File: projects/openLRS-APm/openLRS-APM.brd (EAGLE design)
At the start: 43.1 x 21.8 mm, 23 parts, among them IC2 RFM23BPSMD, J1 AVR_SPI_PRG_6PTH, U1 ATMEGA328P, X2 SMA-142-0711-821/826, Y1 16MHz

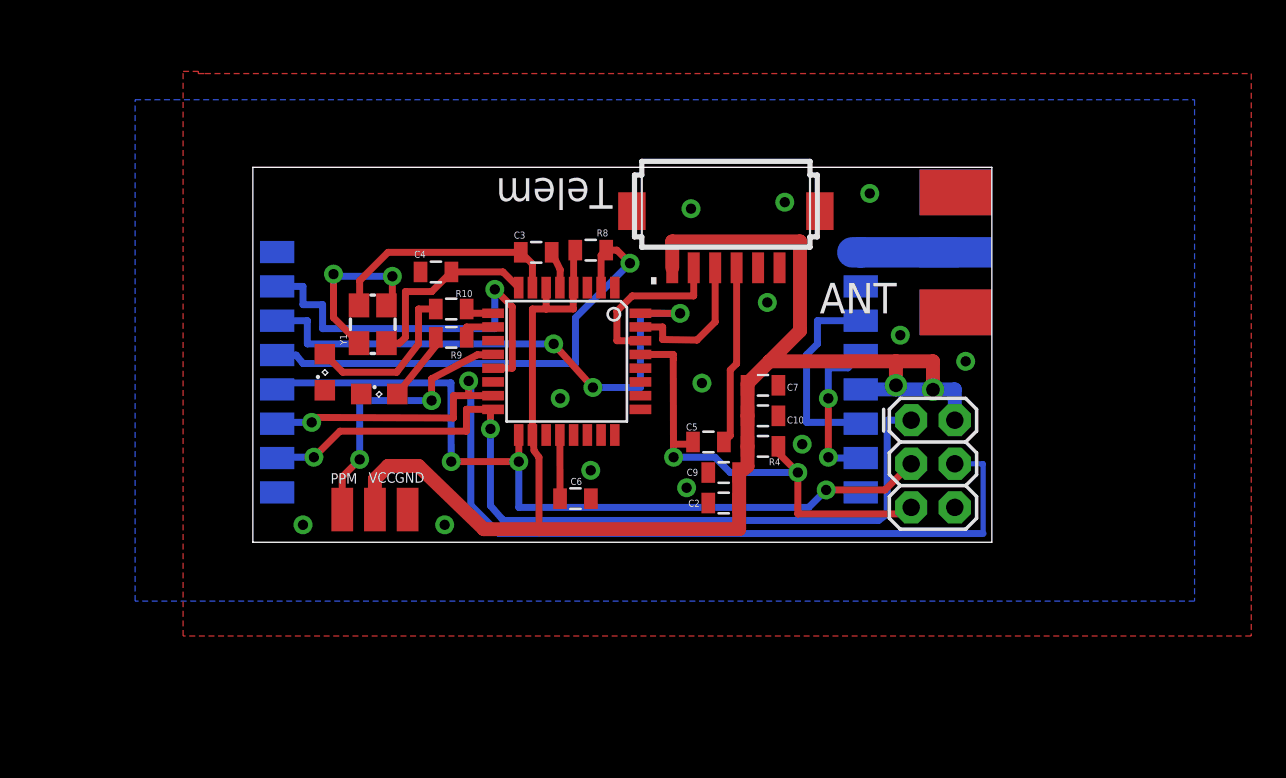
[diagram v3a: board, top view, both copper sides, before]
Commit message: Hopefully Final Revision
Added Documentation and replaced SMA with adafruit SMA. Board shrunk,
and OSH logos added. ready for production. (I HOPE)
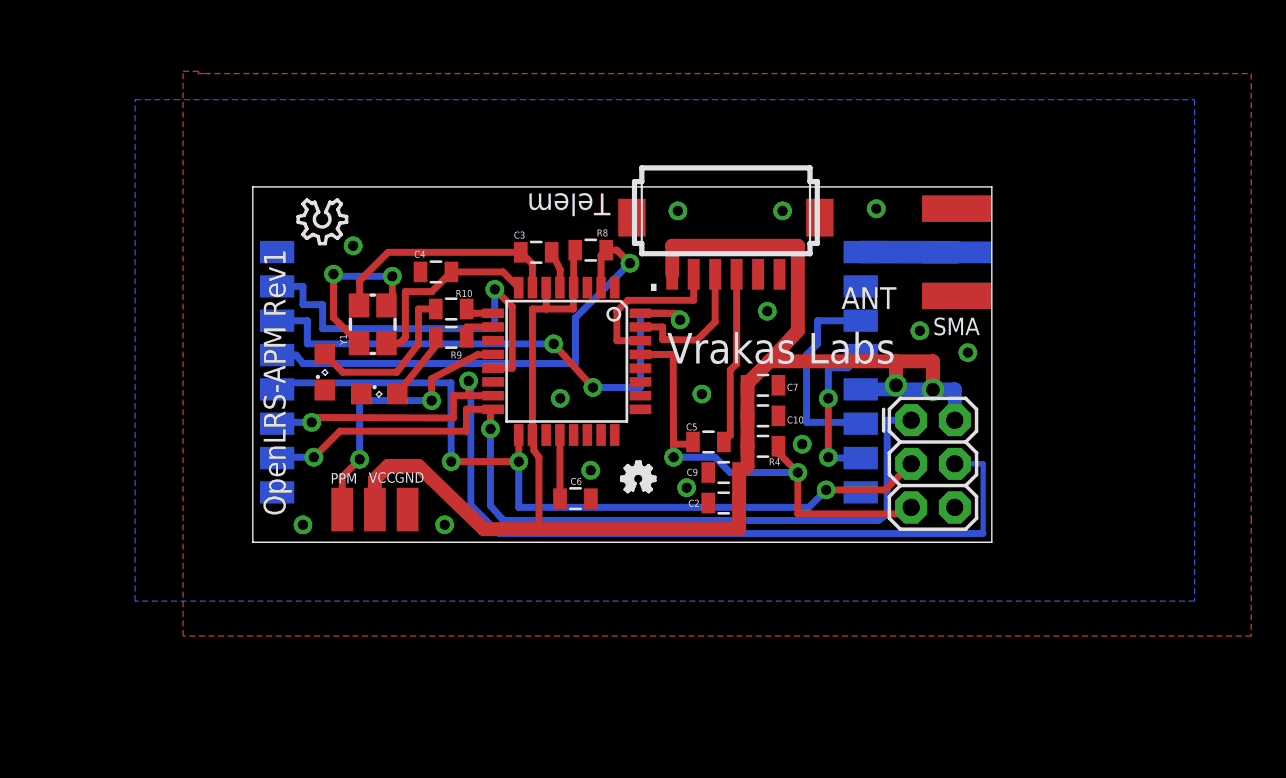
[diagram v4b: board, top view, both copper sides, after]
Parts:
- removed X2: SMA-142-0711-821/826, con-coax:J502-ND-142-0711-821/826
- added SMA: (no value), adafruit:SMA_EDGELAUNCH
- added U$1: (no value), ohw-logo:OSHW_FILLX70_NOTEXT
- added U$2, U$3: (no value), ohw-logo:OSHW_8X100_NOTEXT
- moved TELEMETRY 0.38 mm to (27.6, 16.5)
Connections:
- net GND: now also SMA.GND@1, SMA.GND@2, SMA.GND@3, SMA.GND@4; no longer X2.G@1, X2.G@2, X2.G@3, X2.G@4
- net N$13: now also SMA.P; no longer X2.1
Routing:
- net RF_IRQ: track 32.6 -> 33.4 mm
- net GND: vias 15 -> 16
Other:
- board size 43.1 x 21.8 mm -> 43.1 x 20.7 mm
- board text added: "OpenLRS-APM Rev1"
- board text added: "Vrakas Labs"
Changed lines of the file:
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@@
 <layer number="49" name="Reference" color="7" fill="1" visible="no" active="yes"/>
 <layer number="50" name="dxf" color="7" fill="1" visible="no" active="no"/>
-<layer number="51" name="tDocu" color="7" fill="1" visible="no" active="yes"/>
-<layer number="52" name="bDocu" color="7" fill="1" visible="no" active="yes"/>
+<layer number="51" name="tDocu" color="7" fill="1" visible="yes" active="yes"/>
+<layer number="52" name="bDocu" color="7" fill="1" visible="yes" active="yes"/>
 <layer number="53" name="tGND_GNDA" color="7" fill="9" visible="no" active="no"/>
 <layer number="54" name="bGND_GNDA" color="1" fill="9" visible="no" active="no"/>
@@
 <board>
 <plain>
-<wire x1="0" y1="0" x2="0" y2="21.844" width="0" layer="20"/>
+<wire x1="0" y1="0" x2="0" y2="20.701" width="0" layer="20"/>
 <wire x1="0" y1="0" x2="43.053" y2="0" width="0" layer="20"/>
-<wire x1="43.053" y1="21.844" x2="0" y2="21.844" width="0" layer="20"/>
-<wire x1="43.053" y1="0" x2="43.053" y2="21.844" width="0" layer="20"/>
-<text x="20.955" y="21.209" size="1.778" layer="25" rot="SR180">Telem</text>
-<text x="33.02" y="13.335" size="1.778" layer="25">ANT</text>
-<text x="35.941" y="18.923" size="1.27" layer="26" rot="MR270">1</text>
+<wire x1="43.053" y1="20.701" x2="0" y2="20.701" width="0" layer="20"/>
+<wire x1="43.053" y1="0" x2="43.053" y2="20.701" width="0" layer="20"/>
+<text x="20.828" y="20.32" size="1.27" layer="25" rot="SR180">Telem</text>
+<text x="34.29" y="13.589" size="1.27" layer="25">ANT</text>
+<text x="36.576" y="18.669" size="1.27" layer="26" rot="MR270">1</text>
+<text x="24.13" y="10.414" size="1.778" layer="21">Vrakas Labs</text>
+<text x="1.905" y="1.524" size="1.27" layer="21" rot="R90">OpenLRS-APM Rev1</text>
 </plain>
 <attributes>
@@
 <attribute name="VALUE" x="26.035" y="1.905" size="0.4064" layer="27" rot="R180"/>
 </element>
-<element name="TELEMETRY" library="con-hirose-df13" package="DF13A-6P-1.25H" value="DF13-6P-1.25H" x="27.559" y="16.891"/>
-<element name="X2" library="con-coax" package="J502-ND-142-0711-821/826" value="SMA-142-0711-821/826" x="43.053" y="16.891" smashed="yes" rot="MR0">
-<attribute name="OC_NEWARK" value="16F3627" x="43.053" y="16.891" size="1.778" layer="28" rot="MR0" display="off"/>
-<attribute name="MPN" value="142-0711-821" x="43.053" y="16.891" size="1.778" layer="28" rot="MR0" display="off"/>
-<attribute name="MF" value="JOHNSON COMPONENTS" x="43.053" y="16.891" size="1.778" layer="28" rot="MR0" display="off"/>
-<attribute name="OC_FARNELL" value="1019328" x="43.053" y="16.891" size="1.778" layer="28" rot="MR0" display="off"/>
-</element>
+<element name="TELEMETRY" library="con-hirose-df13" package="DF13A-6P-1.25H" value="DF13-6P-1.25H" x="27.559" y="16.51"/>
 <element name="PPM" library="wirepad" package="SMD1,27-2,54" value="" x="5.207" y="1.905" smashed="yes">
 <attribute name="VALUE" x="5.207" y="1.905" size="0.0254" layer="27"/>
@@
 <attribute name="NAME" x="8.268" y="3.467" size="0.6096" layer="25"/>
 </element>
+<element name="SMA" library="adafruit" package="SMA_EDGELAUNCH" value="" x="43.053" y="16.891" smashed="yes" rot="MR0">
+<attribute name="NAME" x="39.624" y="12.065" size="1.016" layer="25" ratio="18"/>
+<attribute name="VALUE" x="37.973" y="9.271" size="0.8128" layer="28" ratio="10" rot="MR180"/>
+</element>
+<element name="U$1" library="ohw-logo" package="OSHW_FILLX70_NOTEXT" value="" x="21.463" y="2.921"/>
+<element name="U$2" library="ohw-logo" package="OSHW_8X100_NOTEXT" value="" x="5.461" y="19.939" rot="R180"/>
+<element name="U$3" library="ohw-logo" package="OSHW_8X100_NOTEXT" value="" x="2.667" y="19.939" rot="MR180"/>
 </elements>
 <signals>
@@
 <contactref element="LED2" pad="C"/>
 <contactref element="C2" pad="2"/>
-<contactref element="X2" pad="G@2"/>
-<contactref element="X2" pad="G@4"/>
-<contactref element="X2" pad="G@1"/>
-<contactref element="X2" pad="G@3"/>
 <contactref element="GND" pad="1"/>
 <wire x1="1.415" y1="16.891" x2="1.415" y2="16.906" width="0.2032" layer="16"/>
@@
 <via x="11.176" y="1.016" extent="1-16" drill="0.6"/>
 <via x="2.921" y="1.016" extent="1-16" drill="0.6"/>
-<via x="26.162" y="9.271" extent="1-16" drill="0.6"/>
-<via x="41.529" y="10.541" extent="1-16" drill="0.6"/>
-<via x="35.941" y="20.32" extent="1-16" drill="0.6"/>
+<via x="26.162" y="8.636" extent="1-16" drill="0.6"/>
+<via x="41.656" y="11.049" extent="1-16" drill="0.6"/>
+<via x="36.322" y="19.431" extent="1-16" drill="0.6"/>
 <via x="17.907" y="8.382" extent="1-16" drill="0.6"/>
-<via x="29.972" y="13.97" extent="1-16" drill="0.6"/>
-<via x="30.988" y="19.812" extent="1-16" drill="0.6"/>
-<via x="25.527" y="19.431" extent="1-16" drill="0.6"/>
+<via x="29.972" y="13.462" extent="1-16" drill="0.6"/>
+<via x="30.861" y="19.304" extent="1-16" drill="0.6"/>
+<via x="24.765" y="19.304" extent="1-16" drill="0.6"/>
 <wire x1="17.888" y1="14.8336" x2="17.907" y2="15.875" width="0.4064" layer="1"/>
 <wire x1="17.907" y1="15.875" x2="17.41" y2="16.891" width="0.4064" layer="1"/>
 <via x="25.273" y="3.175" extent="1-16" drill="0.6"/>
-<via x="37.719" y="12.065" extent="1-16" drill="0.6"/>
+<via x="38.862" y="12.319" extent="1-16" drill="0.6"/>
 <polygon width="0.4064" layer="1">
 <vertex x="-2.794" y="27.305"/>
@@
 <wire x1="4.699" y1="15.621" x2="4.826" y2="15.494" width="0.4064" layer="16"/>
 <wire x1="4.826" y1="15.494" x2="8.128" y2="15.494" width="0.4064" layer="16"/>
+<contactref element="SMA" pad="GND@1"/>
+<contactref element="SMA" pad="GND@3"/>
+<contactref element="SMA" pad="GND@4"/>
+<contactref element="SMA" pad="GND@2"/>
+<via x="5.842" y="17.272" extent="1-16" drill="0.6"/>
 </signal>
 <signal name="VCC">
@@
 <wire x1="37.465" y1="9.144" x2="37.465" y2="10.541" width="0.8128" layer="1"/>
 <wire x1="37.465" y1="10.541" x2="30.099" y2="10.541" width="0.8128" layer="1"/>
-<wire x1="30.099" y1="10.541" x2="31.877" y2="12.319" width="0.8128" layer="1"/>
-<wire x1="31.877" y1="12.319" x2="31.877" y2="17.526" width="0.8128" layer="1"/>
-<wire x1="31.877" y1="17.526" x2="24.434" y2="17.526" width="0.8128" layer="1"/>
+<wire x1="30.099" y1="10.541" x2="31.75" y2="12.319" width="0.8128" layer="1"/>
+<wire x1="31.75" y1="12.319" x2="31.75" y2="17.272" width="0.8128" layer="1"/>
+<wire x1="31.75" y1="17.272" x2="24.434" y2="17.272" width="0.8128" layer="1"/>
 <wire x1="17.088" y1="13.589" x2="16.288" y2="13.589" width="0.4064" layer="1"/>
 <wire x1="16.288" y1="13.589" x2="16.288" y2="6.2484" width="0.4064" layer="1"/>
@@
 <wire x1="39.624" y1="10.541" x2="37.465" y2="10.541" width="0.8128" layer="1"/>
 <contactref element="TELEMETRY" pad="P$1"/>
-<wire x1="24.434" y1="17.526" x2="24.434" y2="15.991" width="0.8128" layer="1"/>
+<wire x1="24.434" y1="17.272" x2="24.434" y2="15.61" width="0.8128" layer="1"/>
 </signal>
 <signal name="RXD">
 <contactref element="U1" pad="30"/>
-<wire x1="25.684" y1="14.351" x2="22.098" y2="14.351" width="0.4064" layer="1"/>
-<wire x1="22.098" y1="14.351" x2="21.209" y2="13.462" width="0.4064" layer="1"/>
+<wire x1="25.684" y1="14.097" x2="21.844" y2="14.097" width="0.4064" layer="1"/>
+<wire x1="21.844" y1="14.097" x2="21.209" y2="13.462" width="0.4064" layer="1"/>
 <wire x1="22.5806" y1="11.741" x2="21.209" y2="11.741" width="0.4064" layer="1"/>
 <wire x1="21.209" y1="11.741" x2="21.209" y2="13.462" width="0.4064" layer="1"/>
 <contactref element="TELEMETRY" pad="P$2"/>
-<wire x1="25.684" y1="14.351" x2="25.684" y2="15.991" width="0.4064" layer="1"/>
+<wire x1="25.684" y1="14.097" x2="25.684" y2="15.61" width="0.4064" layer="1"/>
 </signal>
 <signal name="TXD">
@@
 <contactref element="TELEMETRY" pad="P$3"/>
 <wire x1="25.876" y1="11.779" x2="26.934" y2="12.837" width="0.4064" layer="1"/>
-<wire x1="26.934" y1="12.837" x2="26.934" y2="15.991" width="0.4064" layer="1"/>
+<wire x1="26.934" y1="12.837" x2="26.934" y2="15.61" width="0.4064" layer="1"/>
 </signal>
 <signal name="DTR">
@@
 <contactref element="TELEMETRY" pad="P$4"/>
 <wire x1="27.813" y1="10.033" x2="28.184" y2="10.404" width="0.4064" layer="1"/>
-<wire x1="28.184" y1="10.404" x2="28.184" y2="15.991" width="0.4064" layer="1"/>
+<wire x1="28.184" y1="10.404" x2="28.184" y2="15.61" width="0.4064" layer="1"/>
 </signal>
 <signal name="/RESET">
@@
 <wire x1="19.812" y1="9.017" x2="22.5806" y2="9.017" width="0.4064" layer="16"/>
 <wire x1="22.5806" y1="9.017" x2="22.5806" y2="13.341" width="0.4064" layer="16"/>
-<wire x1="22.5806" y1="13.341" x2="24.892" y2="13.335" width="0.4064" layer="16"/>
-<via x="24.892" y="13.335" extent="1-16" drill="0.6"/>
-<wire x1="24.892" y1="13.335" x2="22.5806" y2="13.341" width="0.4064" layer="1"/>
+<wire x1="22.5806" y1="13.341" x2="24.638" y2="13.335" width="0.4064" layer="16"/>
+<wire x1="24.638" y1="13.335" x2="24.638" y2="12.954" width="0.4064" layer="16"/>
+<wire x1="24.638" y1="12.954" x2="24.892" y2="12.954" width="0.4064" layer="16"/>
+<via x="24.892" y="12.954" extent="1-16" drill="0.6"/>
+<wire x1="24.892" y1="12.954" x2="24.638" y2="12.954" width="0.4064" layer="1"/>
+<wire x1="24.638" y1="12.954" x2="24.638" y2="13.335" width="0.4064" layer="1"/>
+<wire x1="24.638" y1="13.335" x2="22.5806" y2="13.341" width="0.4064" layer="1"/>
 <wire x1="1.415" y1="12.906" x2="3.175" y2="12.906" width="0.4064" layer="16"/>
 <wire x1="3.175" y1="12.906" x2="3.175" y2="11.557" width="0.4064" layer="16"/>
@@
 <signal name="N$13">
 <contactref element="IC2" pad="1"/>
-<contactref element="X2" pad="1"/>
-<wire x1="40.9376" y1="16.891" x2="35.415" y2="16.891" width="1.778" layer="16"/>
-<wire x1="34.925" y1="16.891" x2="35.415" y2="16.891" width="1.778" layer="16"/>
-<wire x1="35.415" y1="16.891" x2="35.415" y2="16.906" width="1.6764" layer="16"/>
+<contactref element="SMA" pad="P"/>
+<wire x1="35.415" y1="16.906" x2="41.021" y2="16.891" width="1.3208" layer="16"/>
 </signal>
 <signal name="N$24">

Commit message: Final Commit before Rev.1 Fab
Added Logos, Edited designs, Fixed Text
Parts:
- SMA: value (none) -> (none)
- moved U$2 9.65 mm to (15.1, 20.1)
- moved U$3 1.55 mm to (2.92, 18.4)
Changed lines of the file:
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@@
 <wire x1="43.053" y1="0" x2="43.053" y2="20.701" width="0" layer="20"/>
 <text x="20.828" y="20.32" size="1.27" layer="25" rot="SR180">Telem</text>
-<text x="34.29" y="13.589" size="1.27" layer="25">ANT</text>
+<text x="39.878" y="12.065" size="1.016" layer="25">ANT</text>
 <text x="36.576" y="18.669" size="1.27" layer="26" rot="MR270">1</text>
 <text x="24.13" y="10.414" size="1.778" layer="21">Vrakas Labs</text>
@@
 </element>
 <element name="C5" library="SparkFun-Capacitors" package="0805" value="100n" x="26.543" y="5.842" smashed="yes" rot="R180">
-<attribute name="NAME" x="25.908" y="6.9215" size="0.4064" layer="25" rot="R180"/>
+<attribute name="NAME" x="26.035" y="7.0485" size="0.4064" layer="25" rot="R180"/>
 <attribute name="VALUE" x="27.686" y="6.985" size="0.4064" layer="27" rot="R180"/>
 </element>
@@
 <element name="J1" library="SparkFun-Connectors" package="2X3" value="AVR_SPI_PRG_6PTH" x="38.354" y="7.112" smashed="yes" rot="R270"/>
 <element name="R4" library="SparkFun-Resistors" package="0805" value="10k" x="29.718" y="5.588" smashed="yes" rot="R180">
-<attribute name="NAME" x="30.734" y="4.8895" size="0.4064" layer="25" rot="R180"/>
+<attribute name="NAME" x="30.734" y="4.7625" size="0.4064" layer="25" rot="R180"/>
 <attribute name="VALUE" x="29.845" y="4.826" size="0.4064" layer="27" rot="R180"/>
 </element>
@@
 </element>
 <element name="Y1" library="crystal_3225" package="CRYSTAL-SMD-5X3" value="16MHz" x="6.985" y="12.7" smashed="yes" rot="R90">
-<attribute name="NAME" x="5.48" y="11.495" size="0.4064" layer="25" rot="R90"/>
+<attribute name="NAME" x="5.48" y="11.368" size="0.4064" layer="25" rot="R90"/>
 <attribute name="VALUE" x="5.396" y="12.638" size="0.4064" layer="27" rot="R90"/>
 </element>
 <element name="C9" library="SparkFun-Capacitors" package="0805" value="1uF" x="27.432" y="4.064" smashed="yes" rot="R180">
-<attribute name="NAME" x="25.273" y="3.8735" size="0.4064" layer="25"/>
+<attribute name="NAME" x="25.146" y="3.8735" size="0.4064" layer="25"/>
 <attribute name="VALUE" x="25.019" y="4.318" size="0.4064" layer="27"/>
 </element>
@@
 </element>
 <element name="C2" library="SparkFun-Capacitors" package="0805" value="100n" x="27.432" y="2.286" smashed="yes" rot="R180">
-<attribute name="NAME" x="26.035" y="2.4765" size="0.4064" layer="25" rot="R180"/>
+<attribute name="NAME" x="25.908" y="2.4765" size="0.4064" layer="25" rot="R180"/>
 <attribute name="VALUE" x="26.035" y="1.905" size="0.4064" layer="27" rot="R180"/>
 </element>
@@
 <element name="PPM" library="wirepad" package="SMD1,27-2,54" value="" x="5.207" y="1.905" smashed="yes">
 <attribute name="VALUE" x="5.207" y="1.905" size="0.0254" layer="27"/>
-<attribute name="NAME" x="6.083" y="4.026" size="0.6096" layer="25" rot="R180"/>
+<attribute name="NAME" x="5.956" y="4.026" size="0.6096" layer="25" rot="R180"/>
 </element>
 <element name="VCC" library="wirepad" package="SMD1,27-2,54" value="" x="7.112" y="1.905" smashed="yes" rot="R180">
 <attribute name="VALUE" x="7.112" y="1.905" size="0.0254" layer="27" rot="R180"/>
-<attribute name="NAME" x="6.744" y="3.467" size="0.6096" layer="25"/>
+<attribute name="NAME" x="7.988" y="4.026" size="0.6096" layer="25" rot="R180"/>
 </element>
 <element name="GND" library="wirepad" package="SMD1,27-2,54" value="" x="9.017" y="1.905" smashed="yes" rot="R180">
 <attribute name="VALUE" x="9.017" y="1.905" size="0.0254" layer="27" rot="R180"/>
-<attribute name="NAME" x="8.268" y="3.467" size="0.6096" layer="25"/>
-</element>
-<element name="SMA" library="adafruit" package="SMA_EDGELAUNCH" value="" x="43.053" y="16.891" smashed="yes" rot="MR0">
-<attribute name="NAME" x="39.624" y="12.065" size="1.016" layer="25" ratio="18"/>
-<attribute name="VALUE" x="37.973" y="9.271" size="0.8128" layer="28" ratio="10" rot="MR180"/>
+<attribute name="NAME" x="10.274" y="4.026" size="0.6096" layer="25" rot="R180"/>
+</element>
+<element name="SMA" library="adafruit" package="SMA_EDGELAUNCH" value=" " x="43.053" y="16.891" smashed="yes" rot="MR0">
+<attribute name="VALUE" x="38.608" y="11.43" size="0.8128" layer="28" ratio="10" rot="MR180"/>
 </element>
 <element name="U$1" library="ohw-logo" package="OSHW_FILLX70_NOTEXT" value="" x="21.463" y="2.921"/>
-<element name="U$2" library="ohw-logo" package="OSHW_8X100_NOTEXT" value="" x="5.461" y="19.939" rot="R180"/>
-<element name="U$3" library="ohw-logo" package="OSHW_8X100_NOTEXT" value="" x="2.667" y="19.939" rot="MR180"/>
+<element name="U$2" library="ohw-logo" package="OSHW_8X100_NOTEXT" value="" x="15.113" y="20.066" rot="R180"/>
+<element name="U$3" library="ohw-logo" package="OSHW_8X100_NOTEXT" value="" x="2.921" y="18.415" rot="MR180"/>
 </elements>
 <signals>
@@
 <via x="2.921" y="1.016" extent="1-16" drill="0.6"/>
 <via x="26.162" y="8.636" extent="1-16" drill="0.6"/>
-<via x="41.656" y="11.049" extent="1-16" drill="0.6"/>
+<via x="41.656" y="10.668" extent="1-16" drill="0.6"/>
 <via x="36.322" y="19.431" extent="1-16" drill="0.6"/>
 <via x="17.907" y="8.382" extent="1-16" drill="0.6"/>
@@
 <contactref element="TELEMETRY" pad="P$6"/>
 <contactref element="TELEMETRY" pad="P$5"/>
-<via x="4.699" y="15.621" extent="1-16" drill="0.6"/>
+<via x="4.699" y="14.986" extent="1-16" drill="0.6"/>
 <via x="8.128" y="15.494" extent="1-16" drill="0.6"/>
 <wire x1="7.785" y1="13.8" x2="8.128" y2="13.8" width="0.4064" layer="1"/>
 <wire x1="8.128" y1="13.8" x2="8.128" y2="15.494" width="0.4064" layer="1"/>
 <wire x1="6.185" y1="11.6" x2="4.699" y2="13.086" width="0.4064" layer="1"/>
-<wire x1="4.699" y1="13.086" x2="4.699" y2="15.621" width="0.4064" layer="1"/>
-<wire x1="4.699" y1="15.621" x2="4.826" y2="15.494" width="0.4064" layer="16"/>
-<wire x1="4.826" y1="15.494" x2="8.128" y2="15.494" width="0.4064" layer="16"/>
+<wire x1="4.699" y1="13.086" x2="4.699" y2="14.986" width="0.4064" layer="1"/>
+<wire x1="4.699" y1="14.986" x2="4.699" y2="15.494" width="0.4064" layer="16"/>
+<wire x1="4.699" y1="15.494" x2="8.128" y2="15.494" width="0.4064" layer="16"/>
 <contactref element="SMA" pad="GND@1"/>
 <contactref element="SMA" pad="GND@3"/>
 <contactref element="SMA" pad="GND@4"/>
 <contactref element="SMA" pad="GND@2"/>
-<via x="5.842" y="17.272" extent="1-16" drill="0.6"/>
+<via x="6.731" y="17.78" extent="1-16" drill="0.6"/>
 </signal>
 <signal name="VCC">
